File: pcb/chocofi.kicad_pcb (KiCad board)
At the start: 2 copper layers, 111.3 x 90 mm, 55 parts, among them J1 MJ-4PP-9, J2 OLED, SW10 SW_PUSH, SW11 SW_PUSH, SW12 SW_PUSH, SW14 SW_PUSH, SW15 SW_PUSH, SW16 SW_PUSH, SW17 SW_PUSH, SW18 SW_PUSH, SW19 SW_PUSH, SW2 SW_PUSH, SW20 SW_PUSH, SW21 SW_PUSH, SW3 SW_PUSH, SW4 SW_PUSH, SW5 SW_PUSH, SW6 SW_PUSH, SW8 SW_PUSH, SW9 SW_PUSH, U1 ProMicro

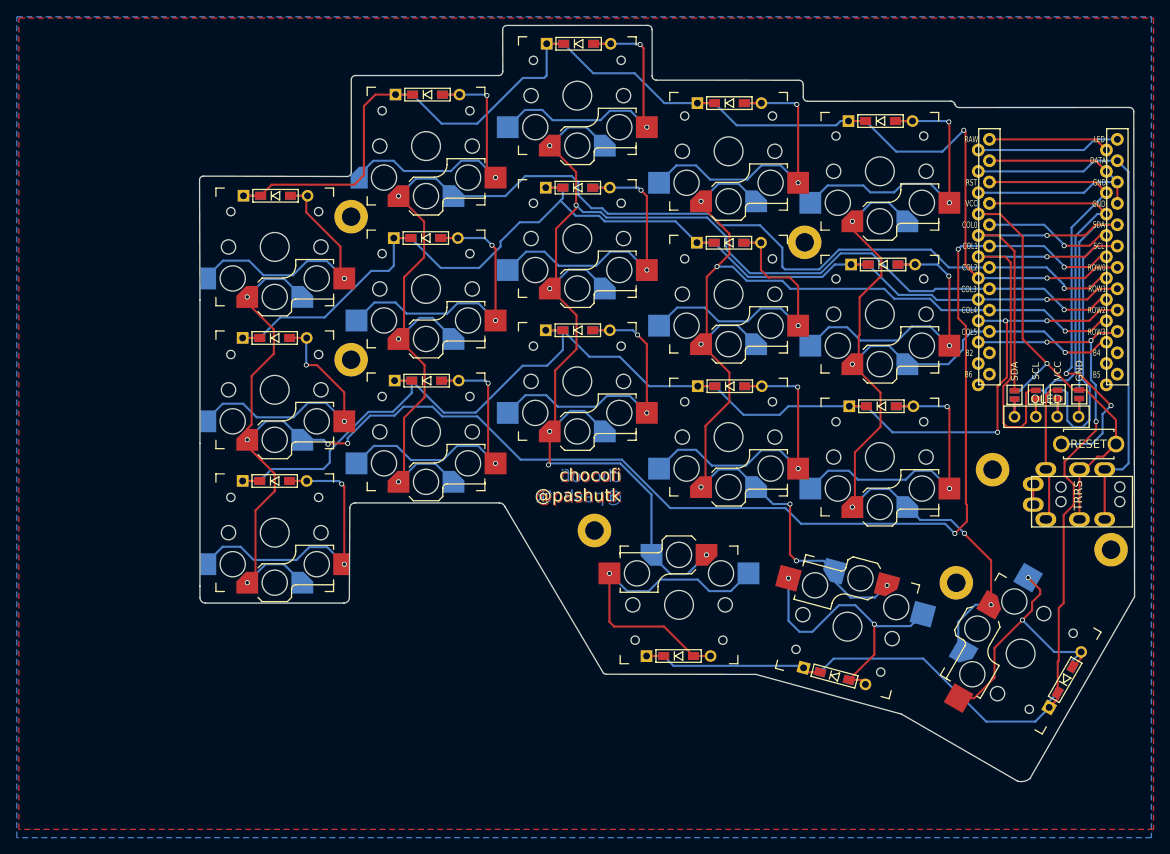
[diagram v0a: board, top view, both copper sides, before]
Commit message: feat: sandwich case mod
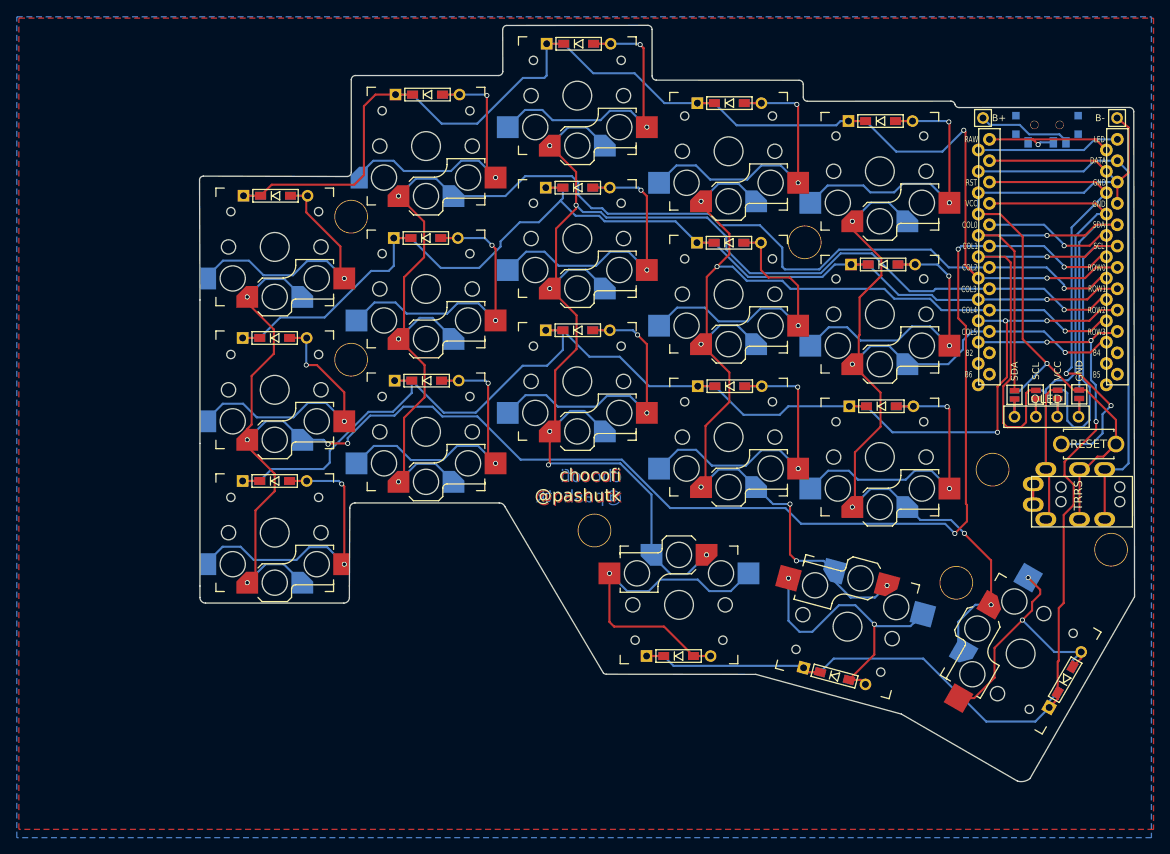
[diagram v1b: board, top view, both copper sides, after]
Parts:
- added B+: MountingHole_Pad, kbd:1pin_conn, F.Cu at (170.2, 55.1)
- added B-: MountingHole_Pad, kbd:1pin_conn, F.Cu at (186.1, 55.1)
- added POWER SW: SW_SPDT, Kailh:SPDT_C128955, B.Cu at (177.8, 55.9)
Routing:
- net bat+: track 0.00 -> 11.2 mm
- net GND: track 91.7 -> 100.6 mm
- net Net-(U1-Pad24): track 14.4 -> 17.3 mm, vias 0 -> 1
